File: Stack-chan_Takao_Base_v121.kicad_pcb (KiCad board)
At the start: 2 copper layers, 25 x 27 mm, 15 parts, among them CN1 CON_USB-C-6, CN2 CON_GROVE, J1 Conn_01x03, J2 Conn_01x03, SW1 SW_SPDT

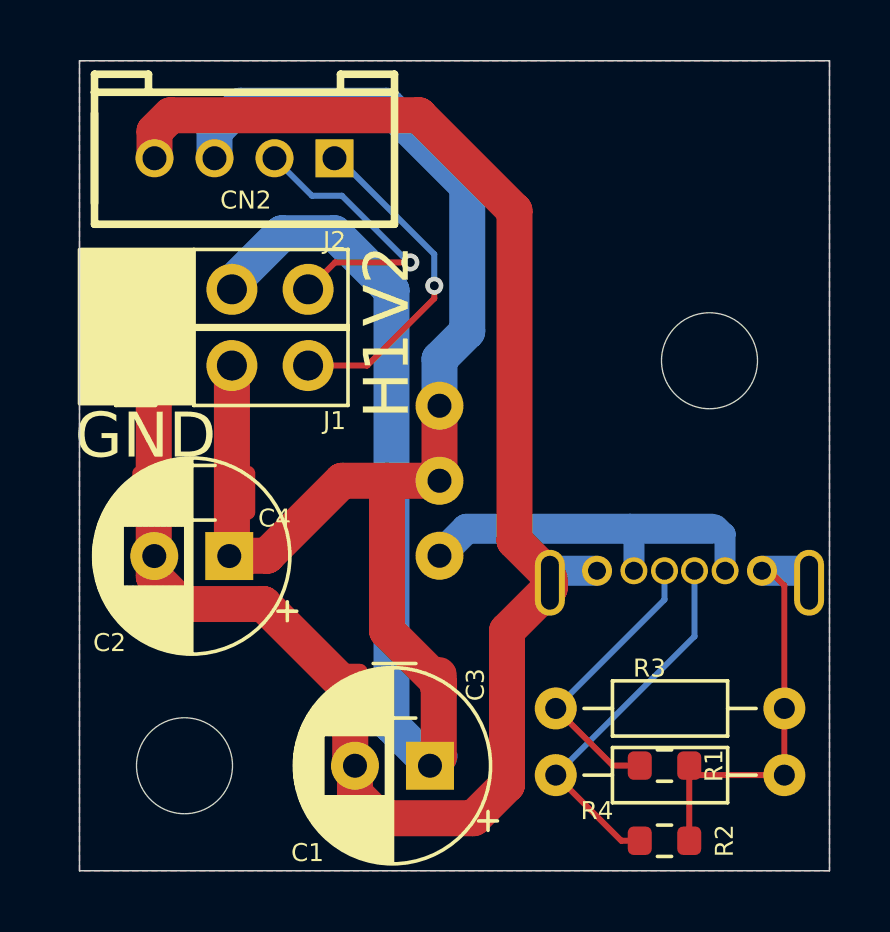
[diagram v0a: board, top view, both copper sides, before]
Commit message: change USB footprint
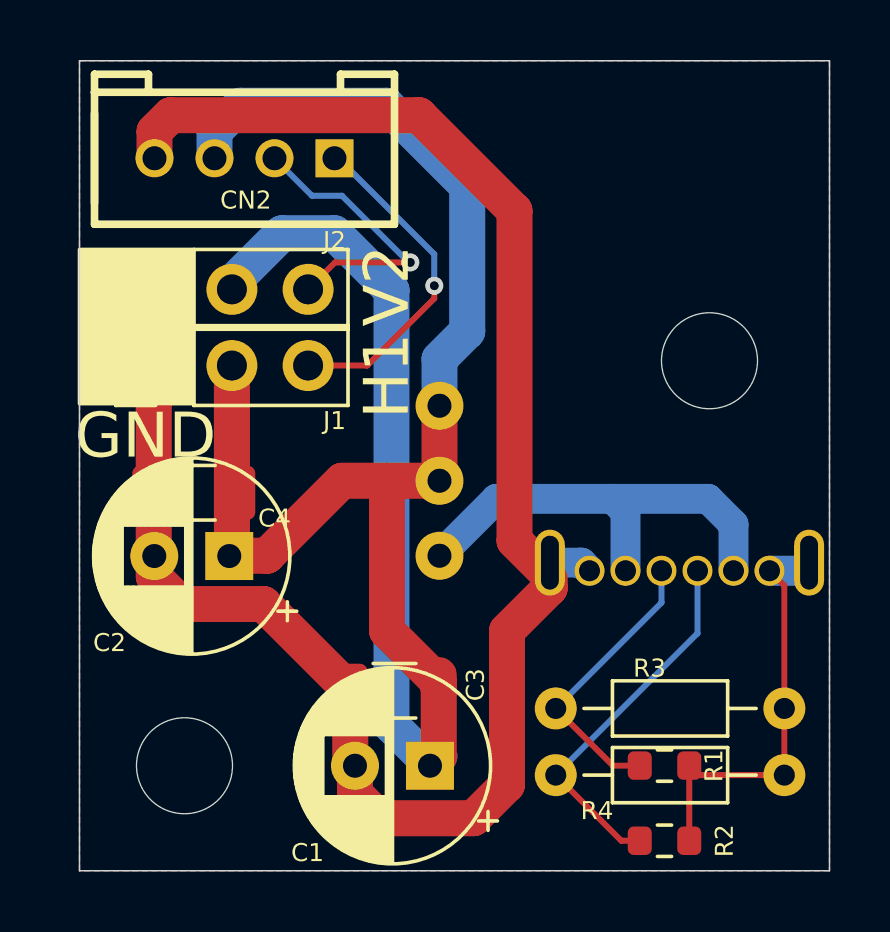
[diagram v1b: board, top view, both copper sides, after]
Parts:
- CN1: footprint akita:USB-C_6P_V_TH2 -> 74th:Connector_USB-C-Receptacle_TH_6-Pin_Vertical
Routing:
- net Net-(CN1-VBUS1): track 12.5 -> 15.1 mm
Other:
- board text added: "v1.21-74th-fork-1"
- board text removed: "v1.21"
